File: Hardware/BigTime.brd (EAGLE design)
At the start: 25.4 x 25.4 mm, 20 parts, among them U2 ATMEGA328P_TQFP, Y1 32.768kHz

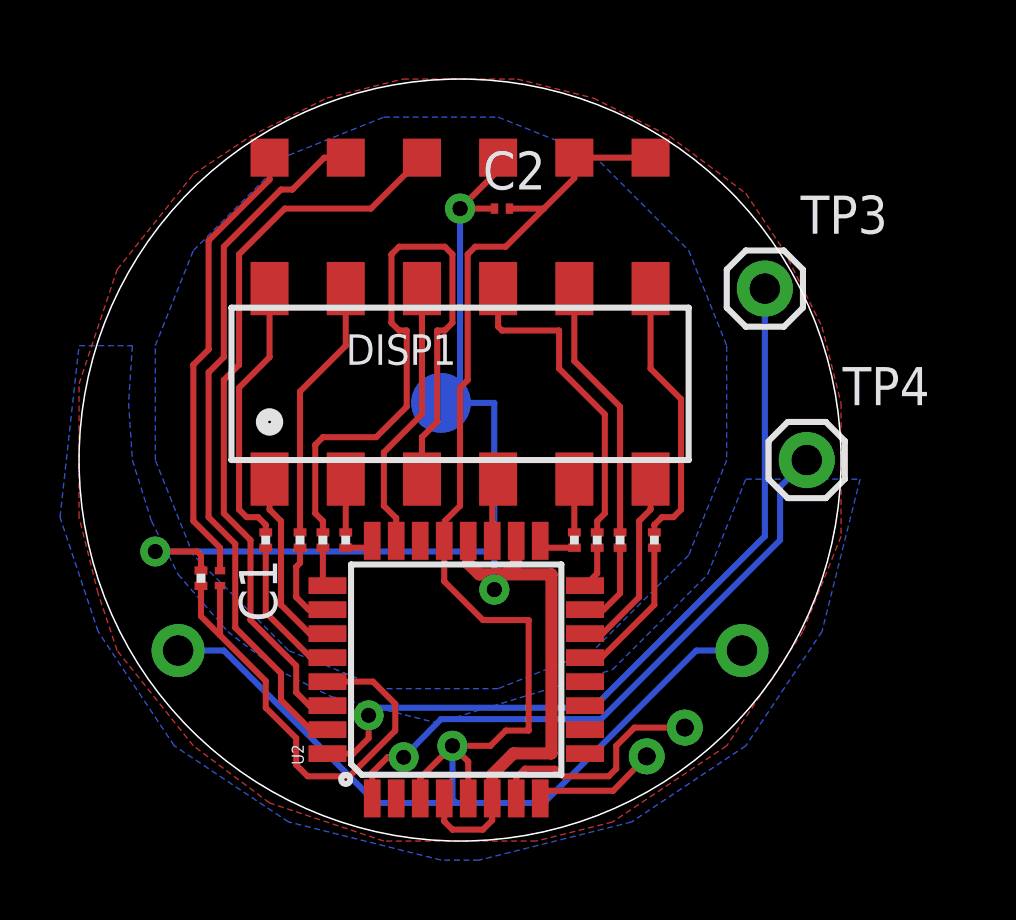
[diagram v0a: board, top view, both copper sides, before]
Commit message: bigger components, no pullup on reset
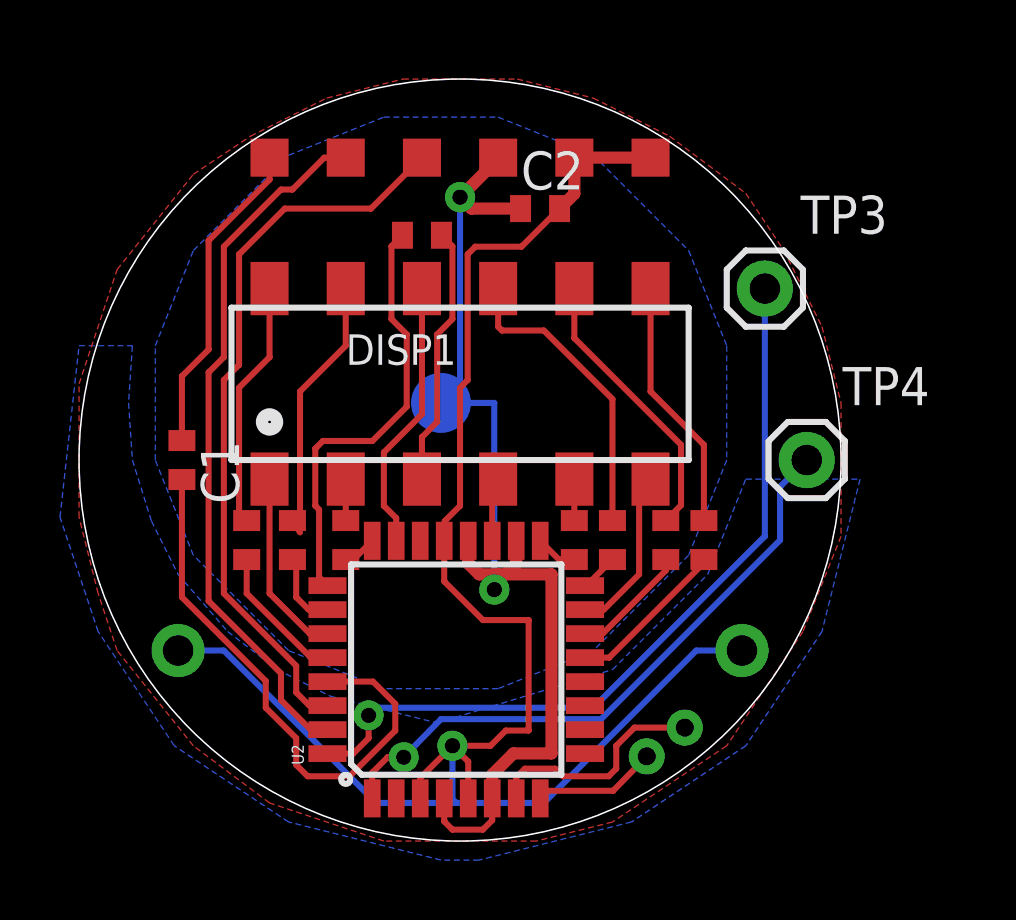
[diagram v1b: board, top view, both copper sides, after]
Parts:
- removed R1: 100k, resistor:R0201
- C1, C2: device resistor:C0201 -> resistor:C0402
- R2, R3, R4, R5, R6, R7, R8, R9: device resistor:R0201 -> resistor:R0402
- moved R4 10.7 mm to (13.3, 24.0), turned to 0 degrees
- moved C1 4.14 mm to (5.33, 16.5)
- moved R8 1.65 mm to (22.7, 13.8)
- moved R5 1.52 mm to (21.5, 13.8)
- moved C2 1.27 mm to (17.3, 24.9)
- moved R2 0.63 mm to (7.49, 13.8)
- moved R7 0.51 mm to (19.7, 13.8)
- moved R3 0.25 mm to (9.02, 13.8)
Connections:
- net D: now also U2.14; no longer U2.15
- net DIG4: now also U2.15; no longer U2.14
- net RST: no longer R1.1
- net VCC: no longer R1.2
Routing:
- net N$6: track 22.3 -> 8.70 mm
- net C: track 1.33 -> 14.4 mm
- net VCC: track 49.4 -> 37.0 mm, vias 3 -> 2
- net N$3: track 15.4 -> 10.8 mm
- net RST: track 16.5 -> 18.6 mm
- net D: track 2.92 -> 3.93 mm
- net N$4: track 9.14 -> 8.26 mm
- net GND: track 59.1 -> 58.3 mm
- net DIG4: track 6.40 -> 5.62 mm
- net N$9: track 10.8 -> 10.1 mm
- net N$10: track 9.14 -> 8.47 mm
- net N$7: track 8.76 -> 9.42 mm

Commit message: rename back to BigTime
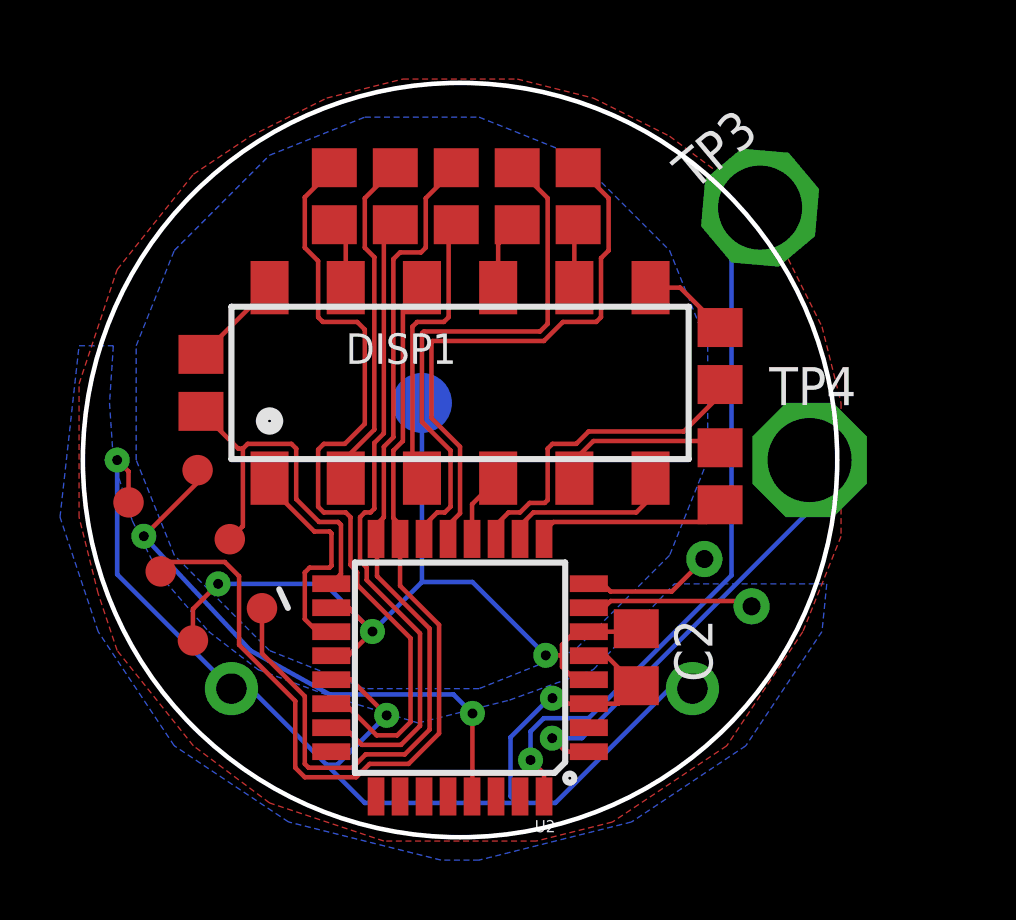
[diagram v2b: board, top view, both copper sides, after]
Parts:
- removed C1: 100nF, resistor:C0402
- removed JP1: FTDI_DEVICERA_SMT, BigTime:FTDI_DEVICE_RA_SMT
- added J1: AVR_SPI_PRG_6TESTPOINTS-SM, Connectors:2X3_TEST_POINTS_SM
- C2: device resistor:C0402 -> resistor:C0805
- R2, R3, R4, R5, R6, R7, R8, R9: device resistor:R0402 -> resistor:R0805
- TP3, TP4: device SparkFun-Connectors:1X01 -> Connectors:WATCHBTN
- moved C2 15.3 mm to (20.5, 9.94), turned to 270 degrees
- moved R7 11.9 mm to (16.5, 25.3), turned to 270 degrees
- moved R5 11.8 mm to (18.5, 25.3), turned to 270 degrees
- moved R6 11.6 mm to (12.4, 25.3)
- moved R3 11.5 mm to (10.4, 25.3), turned to 270 degrees
- moved R8 6.16 mm to (23.3, 20.0)
- moved R2 5.46 mm to (5.97, 19.1)
- moved R9 5.30 mm to (23.3, 16.0)
- moved Y1 4.77 mm to (22.6, 11.5), turned to 225 degrees
- moved TP3 2.70 mm to (24.6, 24.9), turned to 40 degrees
- moved TP5 2.18 mm to (6.99, 8.89)
- moved TP6 2.08 mm to (22.4, 8.89)
- moved R4 1.73 mm to (14.5, 25.3), turned to 270 degrees
- moved BAT+ 0.63 mm to (13.3, 18.4)
- moved U2 0.14 mm to (14.6, 9.59), turned to 180 degrees
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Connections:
- removed net 5: U2.9
- removed net 6: U2.10
- removed net 7: U2.11
- removed net 8: U2.12
- removed net N$3: C1.1, JP1.1
- new net 24: U2.24
- new net 25: U2.25
- new net 26: U2.26
- new net 27: U2.27
- new net 28: U2.28
- net A: now also J1.3, U2.17; no longer U2.28
- net B: now also U2.22; no longer U2.26
- net C: now also J1.1, U2.16; no longer U2.25
- net D: now also U2.13; no longer U2.14
- net DIG1: now also U2.19; no longer U2.27
- net DIG2: now also J1.4, U2.15; no longer U2.23
- net DIG3: now also U2.12; no longer U2.19
- net DIG4: now also U2.10; no longer U2.15
- net DP: now also U2.9; no longer U2.17
- net E: now also U2.23; no longer U2.24
- net F: now also U2.14; no longer U2.16
- net G: now also U2.11; no longer U2.13
- net GND: now also J1.6; no longer JP1.5, JP1.6
- net N$1: now also Y1.1; no longer Y1.2
- net N$2: now also Y1.2; no longer Y1.1
- net RST: now also J1.5; no longer C1.2
- net RXI: no longer JP1.2
- net TXO: no longer JP1.3
- net VCC: now also J1.2; no longer JP1.4
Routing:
- net RXI: track 24.5 -> 0.00 mm
- net B: track 2.69 -> 26.4 mm
- net TXO: track 23.6 -> 0.00 mm
- net DIG2: track 9.10 -> 31.5 mm
- net E: track 1.14 -> 21.6 mm
- net C: track 14.4 -> 31.8 mm
- net F: track 1.27 -> 17.7 mm
- net D: track 3.93 -> 18.6 mm
- net GND: track 58.3 -> 43.6 mm, vias 1 -> 3
- net N$3: track 10.8 -> 0.00 mm
- net N$8: track 1.38 -> 11.3 mm
- net A: track 4.71 -> 12.6 mm
- net N$9: track 10.1 -> 2.36 mm
- net N$7: track 9.42 -> 2.15 mm
- net VCC: track 37.0 -> 29.9 mm, vias 2 -> 3
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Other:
- board size 25.4 x 25.4 mm -> 25.1 x 25.1 mm

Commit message: move crystal and ground pads
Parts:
- moved TP6 4.39 mm to (25.2, 12.2)
- moved Y1 1.43 mm to (22.6, 10.1), turned to 235 degrees
- moved TP5 0.67 mm to (6.51, 8.41)
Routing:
- net GND: track 43.6 -> 33.6 mm, vias 3 -> 5
- net BTN: track 23.9 -> 22.2 mm
- net N$2: track 5.59 -> 6.30 mm
- net SET: track 14.8 -> 15.5 mm
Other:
- outline, holes or cut-outs redrawn

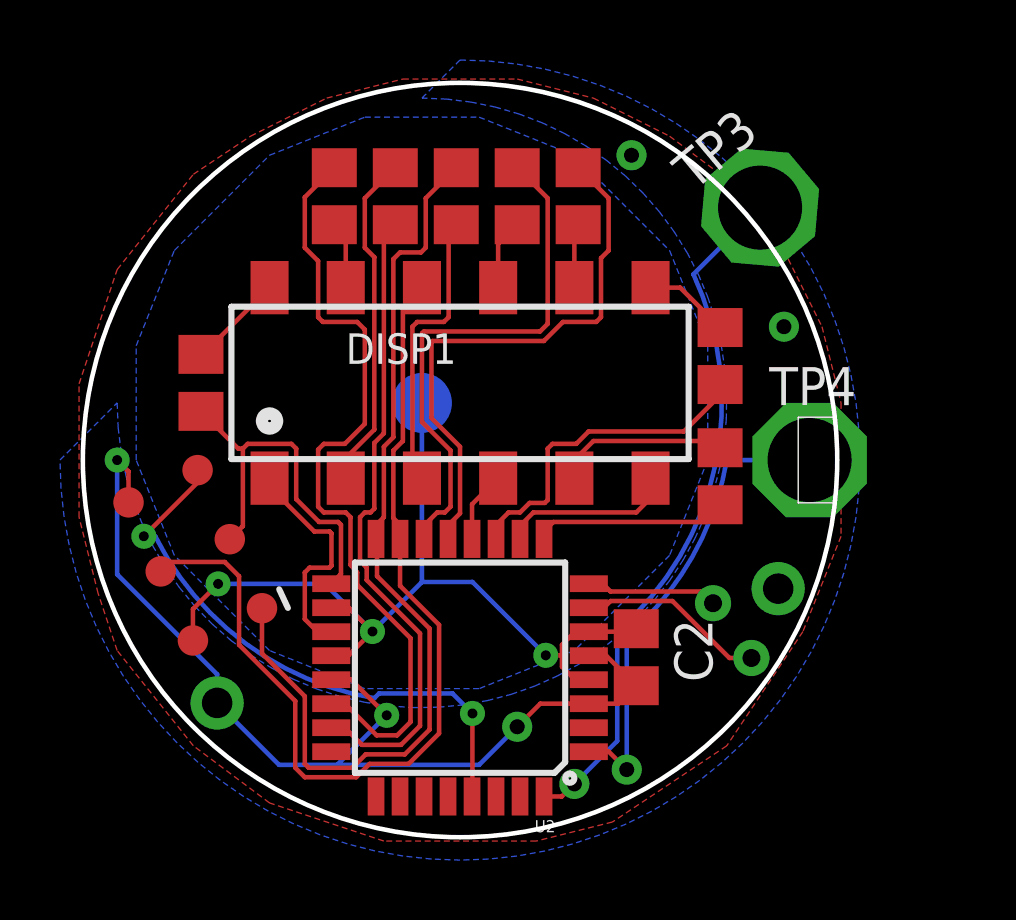
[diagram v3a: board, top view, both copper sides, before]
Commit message: Reroute pins
Can't use A6 and A7 as digital outs
Use bigger traces and more spacing
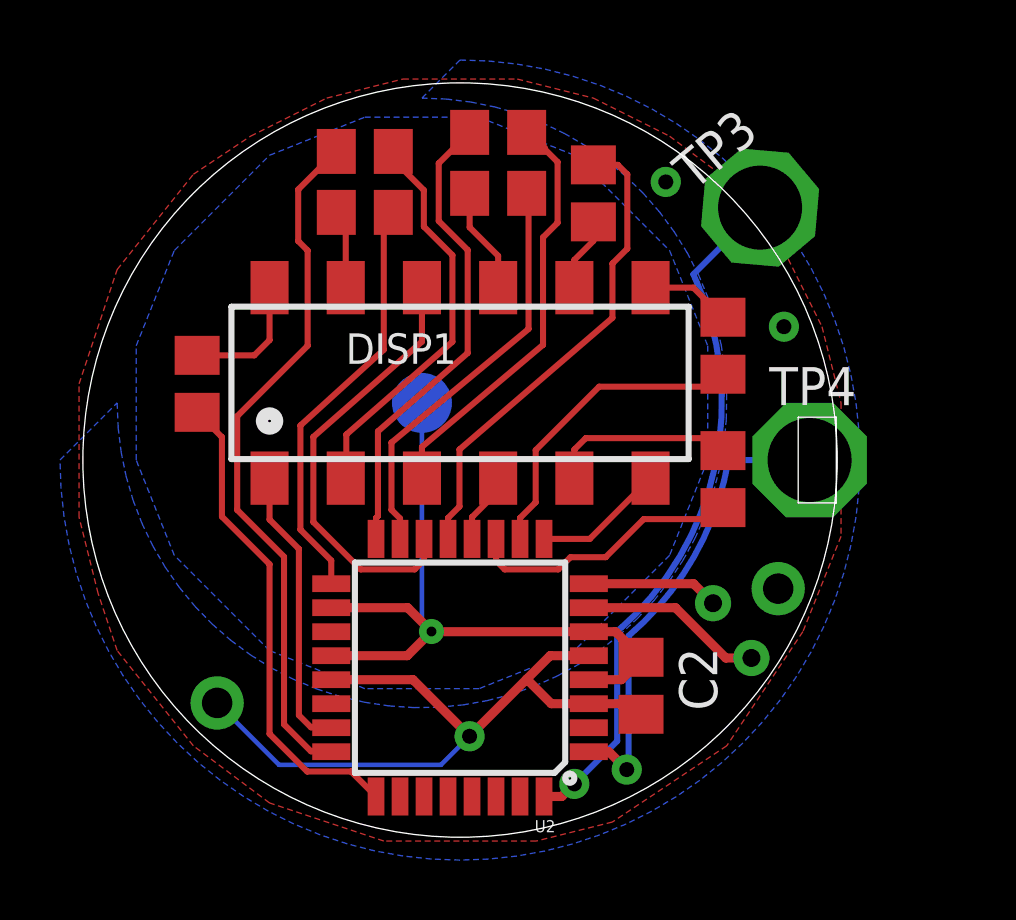
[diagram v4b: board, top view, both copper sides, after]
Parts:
- removed J1: AVR_SPI_PRG_6TESTPOINTS-SM, Connectors:2X3_TEST_POINTS_SM
- moved R4 2.54 mm to (15.9, 27.4), turned to 0 degrees
- moved R6 1.81 mm to (11.4, 26.8), turned to 0 degrees
- moved R3 1.15 mm to (11.4, 24.8), turned to 180 degrees
- moved C2 0.97 mm to (20.6, 8.99)
- moved R7 0.64 mm to (15.9, 25.4), turned to 180 degrees
- moved R5 0.52 mm to (19.1, 25.4)
- moved R8 0.36 mm to (23.4, 20.3)
- moved R9 0.13 mm to (23.4, 15.9)
- moved R2 0.13 mm to (5.84, 19.1)
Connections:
- net N$1 renamed OSC2
- net N$10 renamed G'
- net N$11 renamed DP'
- net N$2 renamed OSC1
- net N$4 renamed A'
- net N$5 renamed B'
- net N$6 renamed C'
- net N$7 renamed D'
- net N$8 renamed E'
- net N$9 renamed F'
- removed net 24: U2.24
- removed net 25: U2.25
- new net 19: U2.19
- new net 2: U2.2
- new net 22: U2.22
- net A: now also U2.25; no longer J1.3, U2.17
- net B: now also U2.17; no longer U2.22
- net C: no longer J1.1
- net DIG1: now also U2.23; no longer U2.19
- net DIG2: now also U2.14; no longer J1.4, U2.15
- net DIG4: now also U2.9; no longer U2.10
- net DP: now also U2.11; no longer U2.9
- net E: now also U2.24; no longer U2.23
- net F: now also U2.15; no longer U2.14
- net G: now also U2.10; no longer U2.11
- net GND: no longer J1.6
- net RST: no longer J1.5
- net VCC: no longer J1.2
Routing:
- net RST: track 18.8 -> 0.00 mm, vias 2 -> 0
- net DIG2: track 31.5 -> 14.7 mm
- net C: track 31.8 -> 15.8 mm
- net B: track 26.4 -> 14.2 mm
- net GND: track 33.6 -> 24.4 mm, vias 5 -> 3
- net C': track 9.71 -> 15.7 mm
- net VCC: track 29.9 -> 24.5 mm, vias 3 -> 1
- net F: track 17.7 -> 13.8 mm
- net A: track 12.6 -> 16.1 mm
- net DP: track 6.53 -> 9.26 mm
- net D: track 18.6 -> 16.1 mm
- net E': track 11.3 -> 13.3 mm
- net DIG1: track 7.67 -> 9.56 mm
- net E: track 21.6 -> 23.4 mm
- net DIG4: track 5.84 -> 4.39 mm
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
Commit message: redesign again
smaller battery, move ic to back, crystal to front, remap pins
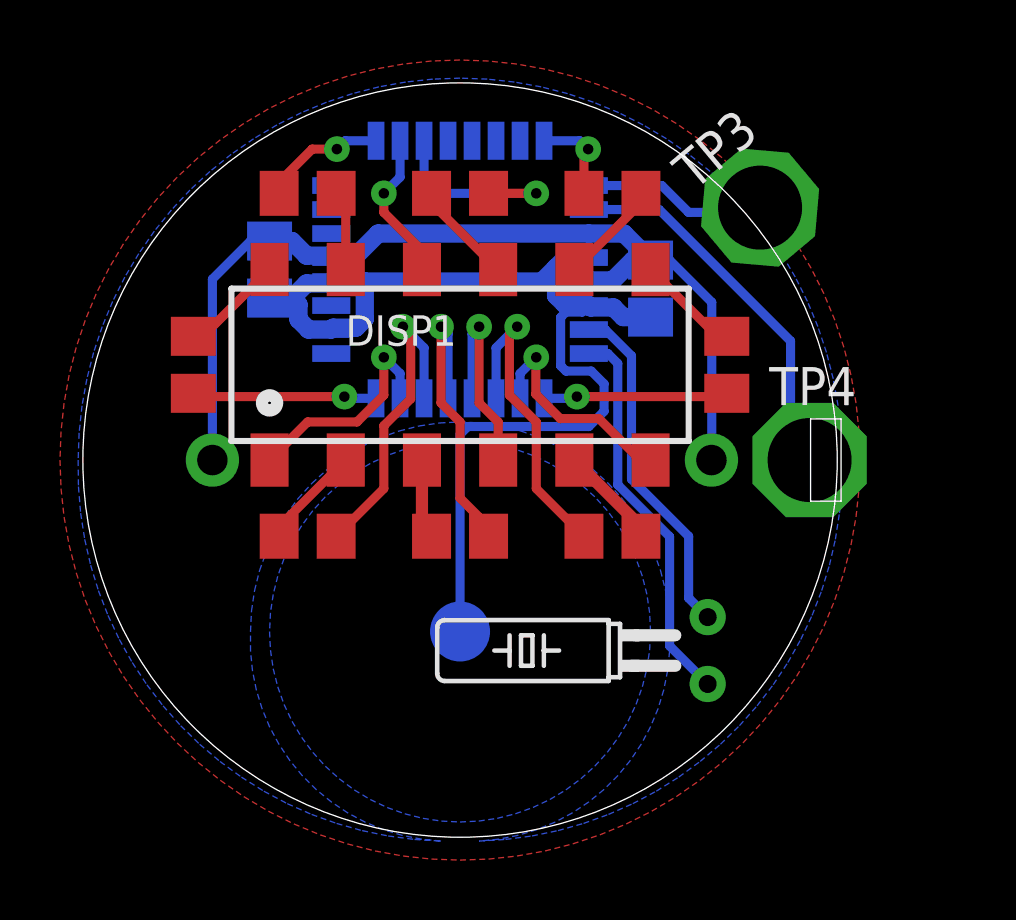
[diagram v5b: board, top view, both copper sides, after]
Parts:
- added C1: 100nF, resistor:C0805
- moved R4 13.5 mm to (14.6, 14.0), turned to 180 degrees
- moved U2 13.3 mm to (14.6, 22.9), flipped to the bottom, turned to 0 degrees
- moved C2 13.2 mm to (21.0, 22.2), flipped to the bottom, turned to 90 degrees
- moved R6 13.0 mm to (9.53, 14.0), turned to 180 degrees
- moved TP5 8.10 mm to (6.35, 16.5)
- moved BAT+ 7.73 mm to (14.6, 10.8)
- moved TP6 4.83 mm to (23.0, 16.5)
- moved R9 4.15 mm to (19.7, 14.0), turned to 0 degrees
- moved R3 2.01 mm to (9.53, 25.4), turned to 0 degrees
- moved R7 1.27 mm to (14.6, 25.4)
- moved Y1 1.05 mm to (21.6, 10.2), flipped to the top, turned to 90 degrees
- moved R8 0.65 mm to (23.5, 19.7)
- moved R2 0.65 mm to (5.71, 19.7)
- moved R5 0.63 mm to (19.7, 25.4), turned to 0 degrees
- moved DISP1 0.60 mm to (14.6, 19.7)
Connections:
- removed net 2: U2.2
- removed net 26: U2.26
- removed net 27: U2.27
- new net 17: U2.17
- new net 23: U2.23
- new net 24: U2.24
- net A: now also U2.16; no longer U2.25
- net B: now also U2.25; no longer U2.17
- net BTN: now also U2.1; no longer U2.32
- net C: now also U2.13; no longer U2.16
- net D: now also U2.32; no longer U2.13
- net DIG1: now also U2.15; no longer U2.23
- net DIG2: now also U2.26; no longer U2.14
- net DIG4: now also U2.10; no longer U2.9
- net E: now also U2.14; no longer U2.24
- net F: now also U2.27; no longer U2.15
- net G: now also U2.9; no longer U2.10
- net GND: now also C1.2
- net SET: now also U2.2; no longer U2.1
- net VCC: now also C1.1
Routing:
- net BTN: track 22.2 -> 6.15 mm, vias 1 -> 0
- net C': track 15.7 -> 2.67 mm
- net D: track 16.1 -> 3.12 mm, vias 0 -> 1
- net VCC: track 24.5 -> 37.2 mm, vias 1 -> 0
- net E: track 23.4 -> 10.8 mm, vias 0 -> 1
- net B: track 14.2 -> 4.18 mm, vias 0 -> 1
- net A: track 16.1 -> 6.16 mm, vias 0 -> 1
- net E': track 13.3 -> 3.46 mm
- net DIG2: track 14.7 -> 5.04 mm, vias 0 -> 1
- net OSC2: track 4.41 -> 13.0 mm
- net GND: track 24.4 -> 32.4 mm, vias 3 -> 0
- net F: track 13.8 -> 6.75 mm, vias 0 -> 1
- net C: track 15.8 -> 10.1 mm, vias 0 -> 1
- net OSC1: track 6.11 -> 11.5 mm
- net DIG3: track 2.39 -> 7.19 mm, vias 0 -> 1
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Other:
- board size 25.1 x 25.1 mm -> 25.3 x 25.1 mm
